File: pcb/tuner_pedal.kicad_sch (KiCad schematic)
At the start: 33 parts, among them U1 STM32F411CEUx, U2 PCM1802DB, U3 MCP1700T-3302E/TT, U4 TPS54302, X1 ECS-2520MVLC-081.92

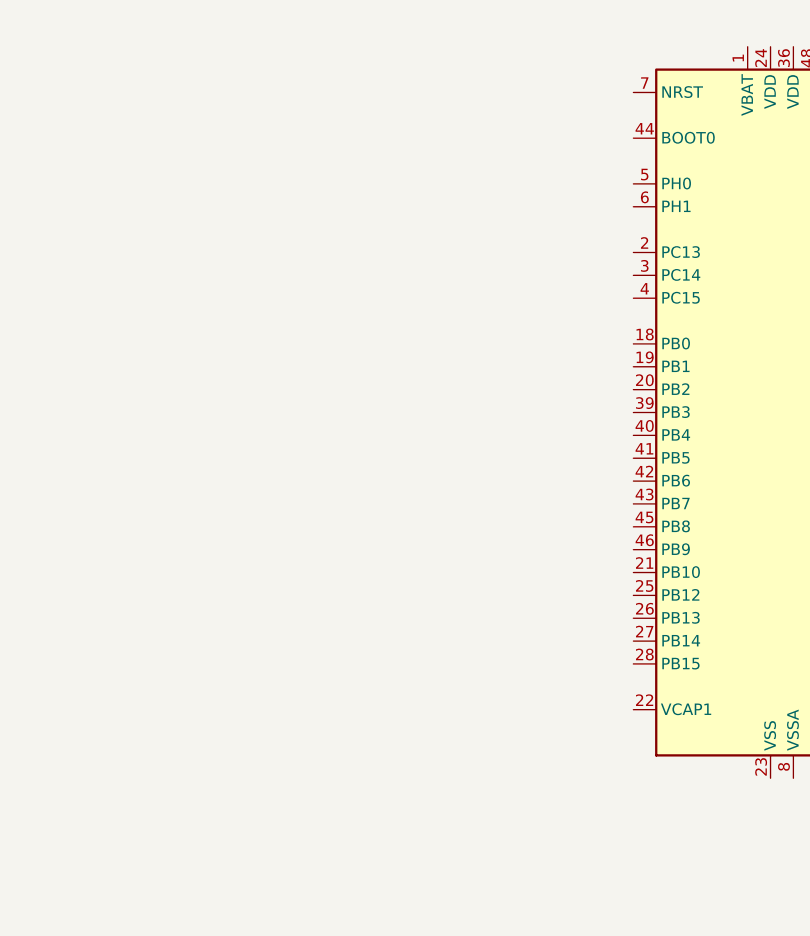
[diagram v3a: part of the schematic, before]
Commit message: Added crystal oscillators to stm32
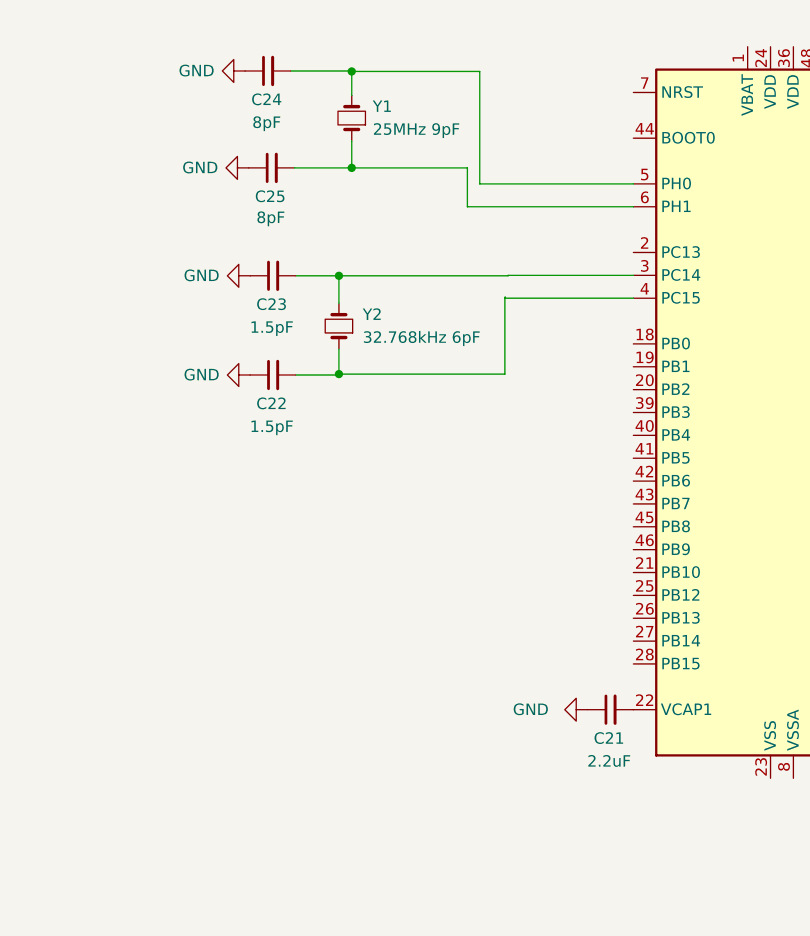
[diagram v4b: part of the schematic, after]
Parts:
- added C21: 2.2uF, symbol Device:C_Small
- added C22, C23: 1.5pF, symbol Device:C_Small
- added C24, C25: 8pF, symbol Device:C_Small
- added Y1: 25MHz 9pF, symbol Device:Crystal_Small
- added Y2: 32.768kHz 6pF, symbol Device:Crystal_Small
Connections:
- net GND: now also C21.1, C22.1, C23.1, C24.1, C25.1
- net at U1.22 (VCAP1): now also C21.2
- net at U1.3 (PC14): now also C23.2, Y2.2
- net at U1.4 (PC15): now also C22.2, Y2.1
- net at U1.5 (PH0): now also C24.2, Y1.2
- net at U1.6 (PH1): now also C25.2, Y1.1

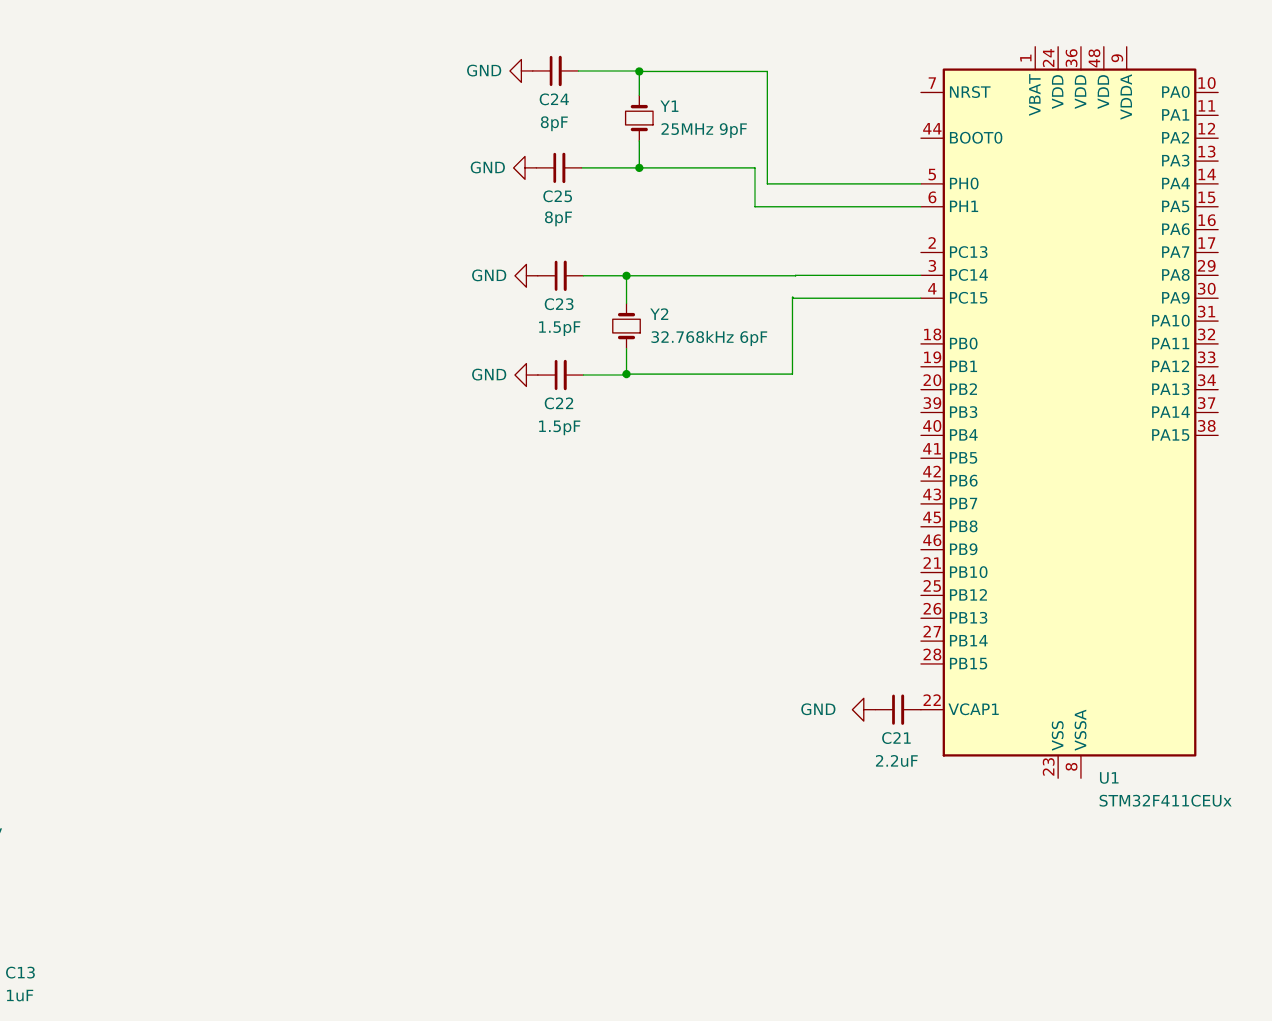
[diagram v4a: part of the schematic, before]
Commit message: Removed RTC crystal
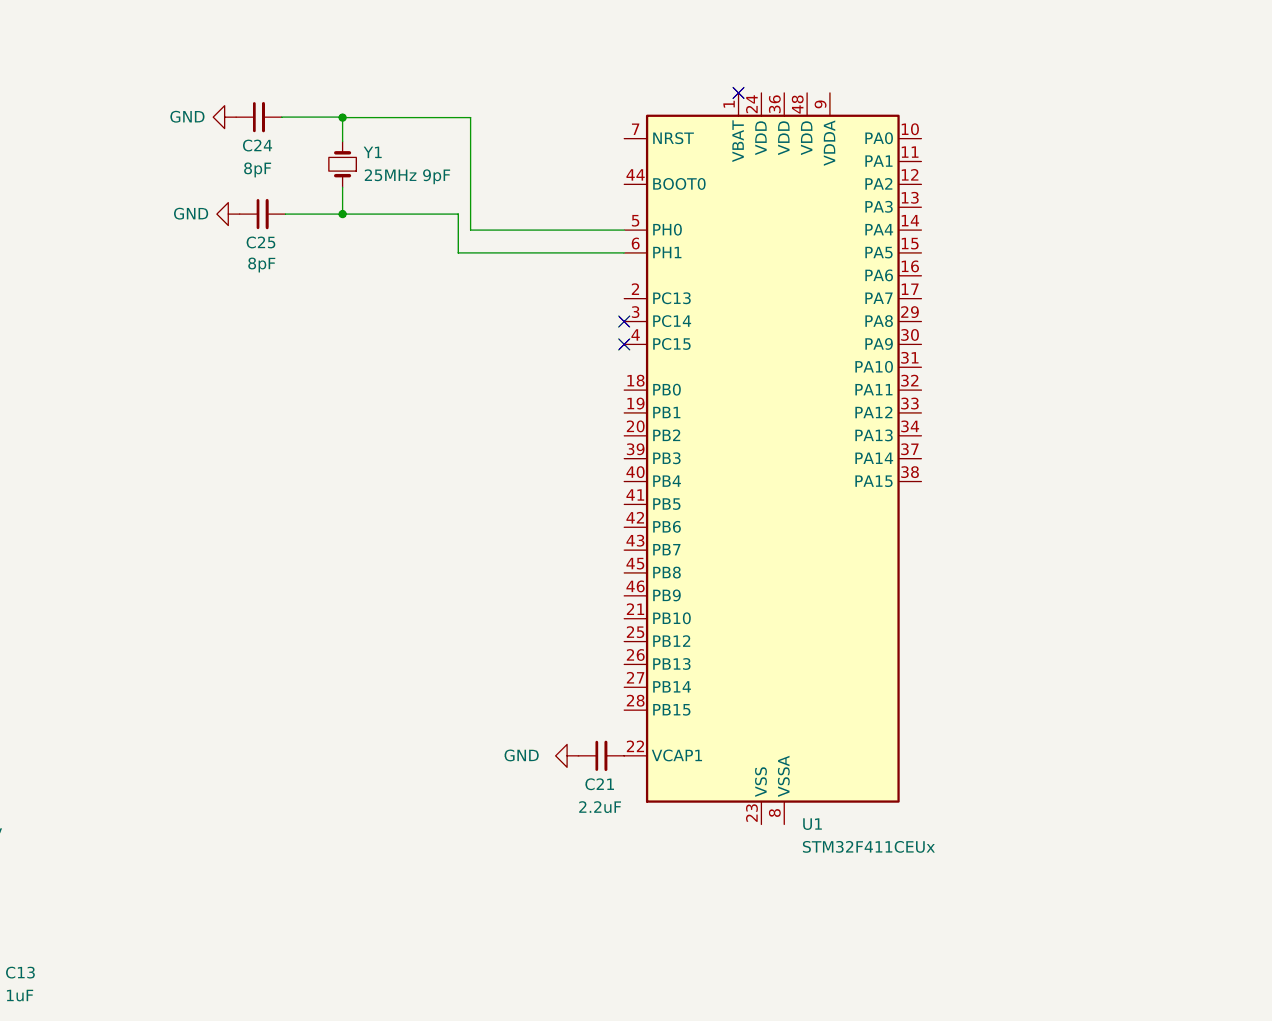
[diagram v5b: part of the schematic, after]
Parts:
- removed C22, C23: 1.5pF, symbol Device:C_Small
- removed Y2: 32.768kHz 6pF, symbol Device:Crystal_Small
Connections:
- no-connect marks 0 -> 3
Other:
- moved on the sheet: C21, C24, C25, U1, Y1

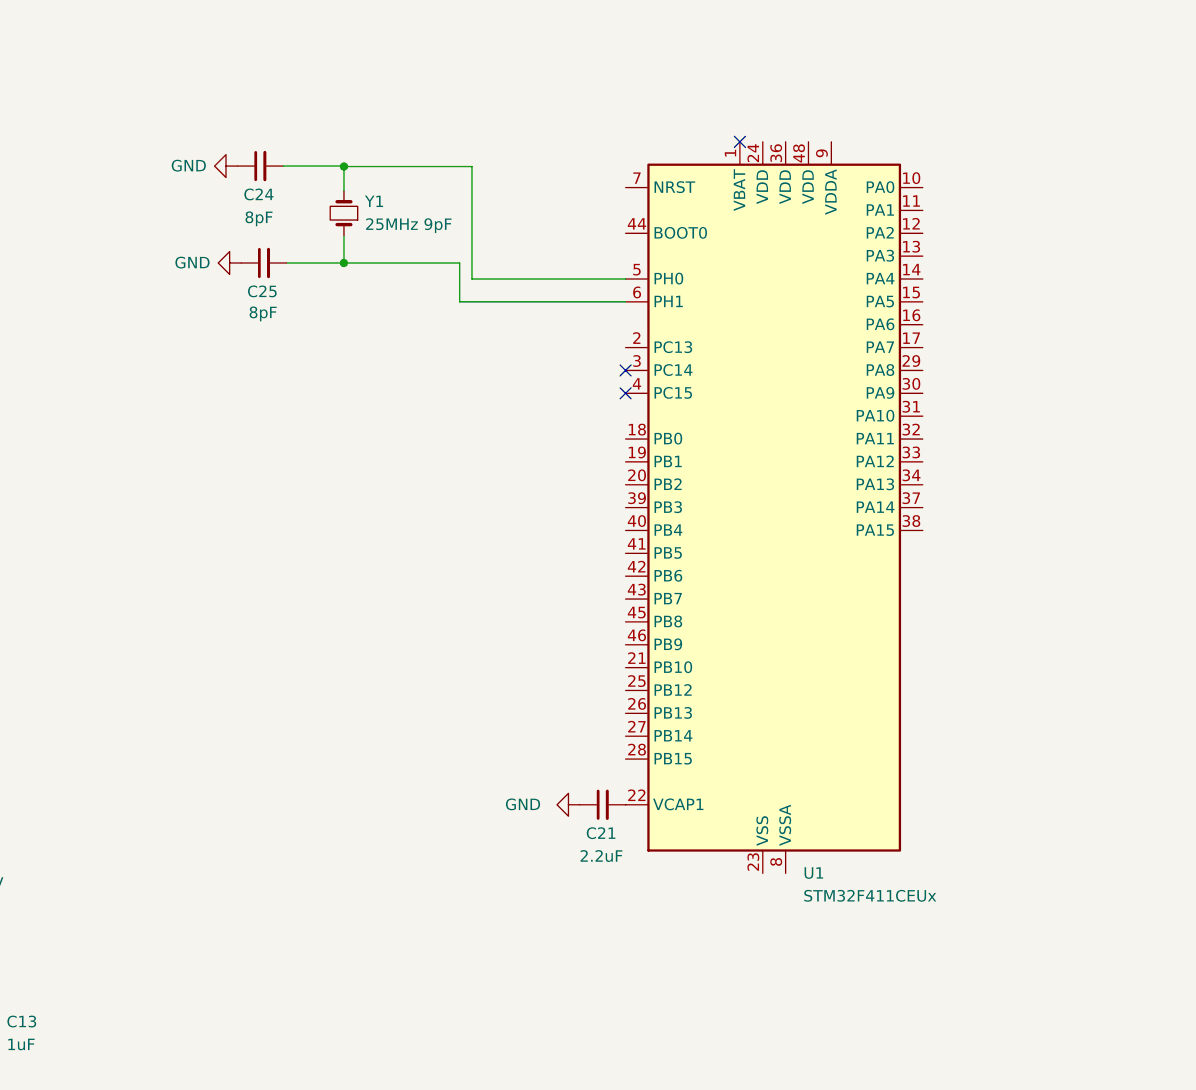
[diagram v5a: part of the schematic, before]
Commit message: Connected stm32 to 3V3
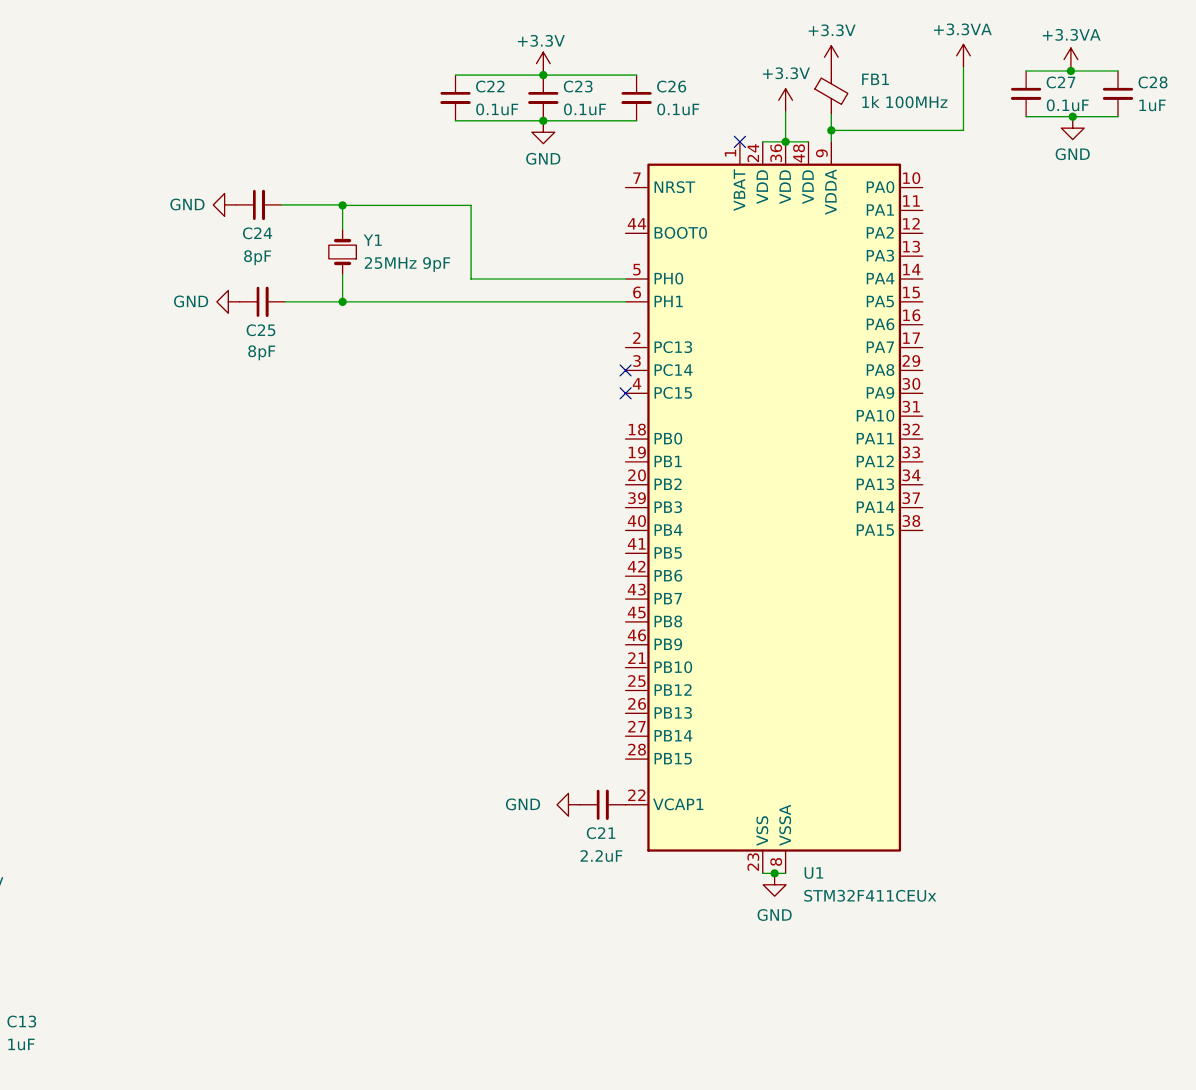
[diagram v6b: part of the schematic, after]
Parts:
- added C22, C23, C26, C27: 0.1uF, symbol Device:C_Small
- added C28: 1uF, symbol Device:C_Small
- added FB1: 1k 100MHz, symbol Device:FerriteBead_Small
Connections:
- net +3.3V: now also U1.24 (VDD), U1.36 (VDD), U1.48 (VDD), C22.1, C23.1, C26.1, FB1.1
- net GND: now also U1.23 (VSS), U1.35 (VSS), U1.47 (VSS), U1.49 (VSS), U1.8 (VSSA), C22.2, C23.2, C26.2, C27.2, C28.2
- net +3.3VA: now reaches U1.9 (VDDA)
- net +3.3VA: now also C27.1, C28.1, FB1.2
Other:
- moved on the sheet: C24, C25, Y1
